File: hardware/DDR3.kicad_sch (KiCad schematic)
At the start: 24 parts, among them U1 NT5CB256M16ER-FL

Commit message: stuff
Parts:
- U1: footprint Package_BGA:FBGA-96_8x13mm_Layout9x16_P0.8mm -> easyeda2kicad:TFBGA-96_L13.0-W8.0-R16-C6-P0.80-TL
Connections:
- net +1V5: now also U1.A2 (DQU5), U1.A3 (DQU7), U1.A7 (DQU4), U1.A9 (VSS), U1.B1 (VSSQ), U1.B3 (VSS), U1.J1 (NC), U1.J2 (VSS), U1.J3 (~{RAS}), U1.J7 (CK), U1.J8 (VSS), U1.J9 (NC), U1.K1 (ODT), U1.K3 (~{CAS_}); no longer U1.C1 (VDDQ), U1.C9 (VDDQ), U1.D2 (VDDQ), U1.D9 (VDD), U1.E9 (VDDQ), U1.F1 (VDDQ), U1.G7 (VDD), U1.H2 (VDDQ), U1.H9 (VDDQ), U1.K8 (VDD), U1.N1 (VDD), U1.N9 (VDD), U1.R1 (VDD), U1.R9 (VDD)
- net A0: now also U1.K8 (VDD); no longer U1.N3 (A0)
- net A1: now also U1.K9 (CKE); no longer U1.P7 (A1)
- net A10: now also U1.M3 (BA2); no longer U1.L7 (A10/AP)
- net A11: now also U1.M7 (NC); no longer U1.R7 (A11)
- net A12: now also U1.M8 (VREFCA); no longer U1.N7 (A12/~{BC})
- net A13: now also U1.M9 (VSS); no longer U1.T3 (A13)
- net A14: now also U1.N1 (VDD); no longer U1.T7 (A14)
- net A2: now also U1.L1 (NC); no longer U1.P3 (A2)
- net A3: now also U1.L2 (~{CS}); no longer U1.N2 (A3)
- net A4: now also U1.L3 (~{WE}); no longer U1.P8 (A4)
- net A5: now also U1.L7 (A10/AP); no longer U1.P2 (A5)
- net A6: now also U1.L8 (ZQ); no longer U1.R8 (A6)
- net A7: now also U1.L9 (NC); no longer U1.R2 (A7)
- net A8: now also U1.M1 (VSS); no longer U1.T8 (A8)
- net A9: now also U1.M2 (BA0); no longer U1.R3 (A9)
- net BA0: no longer U1.M2 (BA0)
- net BA1: no longer U1.N8 (BA1)
- net BA2: no longer U1.M3 (BA2)
- net CASn: no longer U1.K3 (~{CAS_})
- net CKE: no longer U1.K9 (CKE)
- net CKN: no longer U1.K7 (~{CK})
- net CKP: no longer U1.J7 (CK)
- net CSn: no longer U1.L2 (~{CS})
- net DML: no longer U1.E7 (DML)
- net DMU: no longer U1.D3 (DMU)
- net DQL0: now also U1.E1 (VSS); no longer U1.G2 (DQL6)
- net DQL1: now also U1.D9 (VDD); no longer U1.H8 (DQL5)
- net DQL2: now also U1.E2 (VSSQ); no longer U1.H7 (DQL7)
- net DQL3: now also U1.D2 (VDDQ); no longer U1.F7 (DQL1)
- net DQL4: now also U1.D3 (DMU); no longer U1.F2 (DQL2)
- net DQL5: now also U1.D8 (VSSQ); no longer U1.H3 (DQL4)
- net DQL6: now also U1.D1 (VSSQ); no longer U1.E3 (DQL0)
- net DQL7: now also U1.D7 (DQU0); no longer U1.F8 (DQL3)
- net DQSLN: no longer U1.G3 (~{DQSL})
- net DQSLP: no longer U1.F3 (DQSL)
- net DQSUN: no longer U1.B7 (~{DQSU})
- net DQSUP: no longer U1.C7 (DQSU)
- net DQU0: now also U1.C3 (DQU1); no longer U1.A7 (DQU4)
- net DQU1: now also U1.B9 (VSSQ); no longer U1.C3 (DQU1)
- net DQU2: now also U1.C8 (DQU2); no longer U1.B8 (DQU6)
- net DQU4: now also U1.C7 (DQSU); no longer U1.A2 (DQU5)
- net DQU5: now also U1.B8 (DQU6); no longer U1.D7 (DQU0)
- net DQU6: now also U1.C1 (VDDQ); no longer U1.C8 (DQU2)
- net DQU7: now also U1.C9 (VDDQ); no longer U1.A3 (DQU7)
- net GND: no longer U1.A9 (VSS), U1.B1 (VSSQ), U1.B3 (VSS), U1.B9 (VSSQ), U1.D1 (VSSQ), U1.D8 (VSSQ), U1.E1 (VSS), U1.E2 (VSSQ), U1.E8 (VSSQ), U1.F9 (VSSQ), U1.G1 (VSSQ), U1.G8 (VSS), U1.G9 (VSSQ), U1.J1 (NC), U1.J2 (VSS), U1.J8 (VSS), U1.J9 (NC), U1.L1 (NC), U1.L9 (NC), U1.M1 (VSS), U1.M7 (NC), U1.M9 (VSS), U1.P1 (VSS), U1.P9 (VSS), U1.T1 (VSS), U1.T9 (VSS)
- net ODT: no longer U1.K1 (ODT)
- net RASn: no longer U1.J3 (~{RAS})
- net RSTn: no longer U1.T2 (~{RESET})
- net WEn: no longer U1.L3 (~{WE})
- net at C18.2, C19.1, R2.2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: now also U1.N3 (A0); no longer U1.H1 (VREFDQ), U1.M8 (VREFCA)
- net at R1.1: no longer U1.L8 (ZQ)

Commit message: Routing and PCB
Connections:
- net +1V5: now also U1.C1 (VDDQ), U1.C9 (VDDQ), U1.D2 (VDDQ), U1.D9 (VDD), U1.E9 (VDDQ), U1.F1 (VDDQ), U1.G7 (VDD), U1.H2 (VDDQ), U1.H9 (VDDQ), U1.K8 (VDD), U1.N1 (VDD), U1.N9 (VDD), U1.R1 (VDD), U1.R9 (VDD); no longer U1.A2 (DQU5), U1.A3 (DQU7), U1.A7 (DQU4), U1.A9 (VSS), U1.B1 (VSSQ), U1.B3 (VSS), U1.J1 (NC), U1.J2 (VSS), U1.J3 (~{RAS}), U1.J7 (CK), U1.J8 (VSS), U1.J9 (NC), U1.K1 (ODT), U1.K3 (~{CAS_})
- net A0: now also U1.N3 (A0); no longer U1.K8 (VDD)
- net A1: now also U1.P7 (A1); no longer U1.K9 (CKE)
- net A10: now also U1.L7 (A10/AP); no longer U1.M3 (BA2)
- net A11: now also U1.R7 (A11); no longer U1.M7 (NC)
- net A12: now also U1.N7 (A12/~{BC}); no longer U1.M8 (VREFCA)
- net A13: now also U1.T3 (A13); no longer U1.M9 (VSS)
- net A14: now also U1.T7 (A14); no longer U1.N1 (VDD)
- net A2: now also U1.P3 (A2); no longer U1.L1 (NC)
- net A3: now also U1.N2 (A3); no longer U1.L2 (~{CS})
- net A4: now also U1.P8 (A4); no longer U1.L3 (~{WE})
- net A5: now also U1.P2 (A5); no longer U1.L7 (A10/AP)
- net A6: now also U1.R8 (A6); no longer U1.L8 (ZQ)
- net A7: now also U1.R2 (A7); no longer U1.L9 (NC)
- net A8: now also U1.T8 (A8); no longer U1.M1 (VSS)
- net A9: now also U1.R3 (A9); no longer U1.M2 (BA0)
- net BA0: now also U1.M2 (BA0)
- net BA1: now also U1.N8 (BA1)
- net BA2: now also U1.M3 (BA2)
- net CASn: now also U1.K3 (~{CAS})
- net CKE: now also U1.K9 (CKE)
- net CKN: now also U1.K7 (~{CK})
- net CKP: now also U1.J7 (CK)
- net CSn: now also U1.L2 (~{CS})
- net DML: now also U1.E7 (DML)
- net DMU: now also U1.D3 (DMU)
- net DQL0: now also U1.G2 (DQL6); no longer U1.E1 (VSS)
- net DQL1: now also U1.H8 (DQL5); no longer U1.D9 (VDD)
- net DQL2: now also U1.H7 (DQL7); no longer U1.E2 (VSSQ)
- net DQL3: now also U1.F7 (DQL1); no longer U1.D2 (VDDQ)
- net DQL4: now also U1.F2 (DQL2); no longer U1.D3 (DMU)
- net DQL5: now also U1.H3 (DQL4); no longer U1.D8 (VSSQ)
- net DQL6: now also U1.E3 (DQL0); no longer U1.D1 (VSSQ)
- net DQL7: now also U1.F8 (DQL3); no longer U1.D7 (DQU0)
- net DQSLN: now also U1.G3 (~{DQSL})
- net DQSLP: now also U1.F3 (DQSL)
- net DQSUN: now also U1.B7 (~{DQSU})
- net DQSUP: now also U1.C7 (DQSU)
- net DQU0: now also U1.A7 (DQU4); no longer U1.C3 (DQU1)
- net DQU1: now also U1.C3 (DQU1); no longer U1.B9 (VSSQ)
- net DQU2: now also U1.B8 (DQU6); no longer U1.C8 (DQU2)
- net DQU4: now also U1.A2 (DQU5); no longer U1.C7 (DQSU)
- net DQU5: now also U1.D7 (DQU0); no longer U1.B8 (DQU6)
- net DQU6: now also U1.C8 (DQU2); no longer U1.C1 (VDDQ)
- net DQU7: now also U1.A3 (DQU7); no longer U1.C9 (VDDQ)
- net GND: now also U1.A9 (VSS), U1.B1 (VSSQ), U1.B3 (VSS), U1.B9 (VSSQ), U1.D1 (VSSQ), U1.D8 (VSSQ), U1.E1 (VSS), U1.E2 (VSSQ), U1.E8 (VSSQ), U1.F9 (VSSQ), U1.G1 (VSSQ), U1.G8 (VSS), U1.G9 (VSSQ), U1.J1 (NC), U1.J2 (VSS), U1.J8 (VSS), U1.J9 (NC), U1.L1 (NC), U1.L9 (NC), U1.M1 (VSS), U1.M7 (NC), U1.M9 (VSS), U1.P1 (VSS), U1.P9 (VSS), U1.T1 (VSS), U1.T9 (VSS)
- net ODT: now also U1.K1 (ODT)
- net RASn: now also U1.J3 (~{RAS})
- net RSTn: now also U1.T2 (~{RESET})
- net WEn: now also U1.L3 (~{WE})
- net at U1.H1 (VREFDQ): now also C18.2, C19.1, R2.2, R3.1, U1.M8 (VREFCA)
- net at R1.1: now also U1.L8 (ZQ)

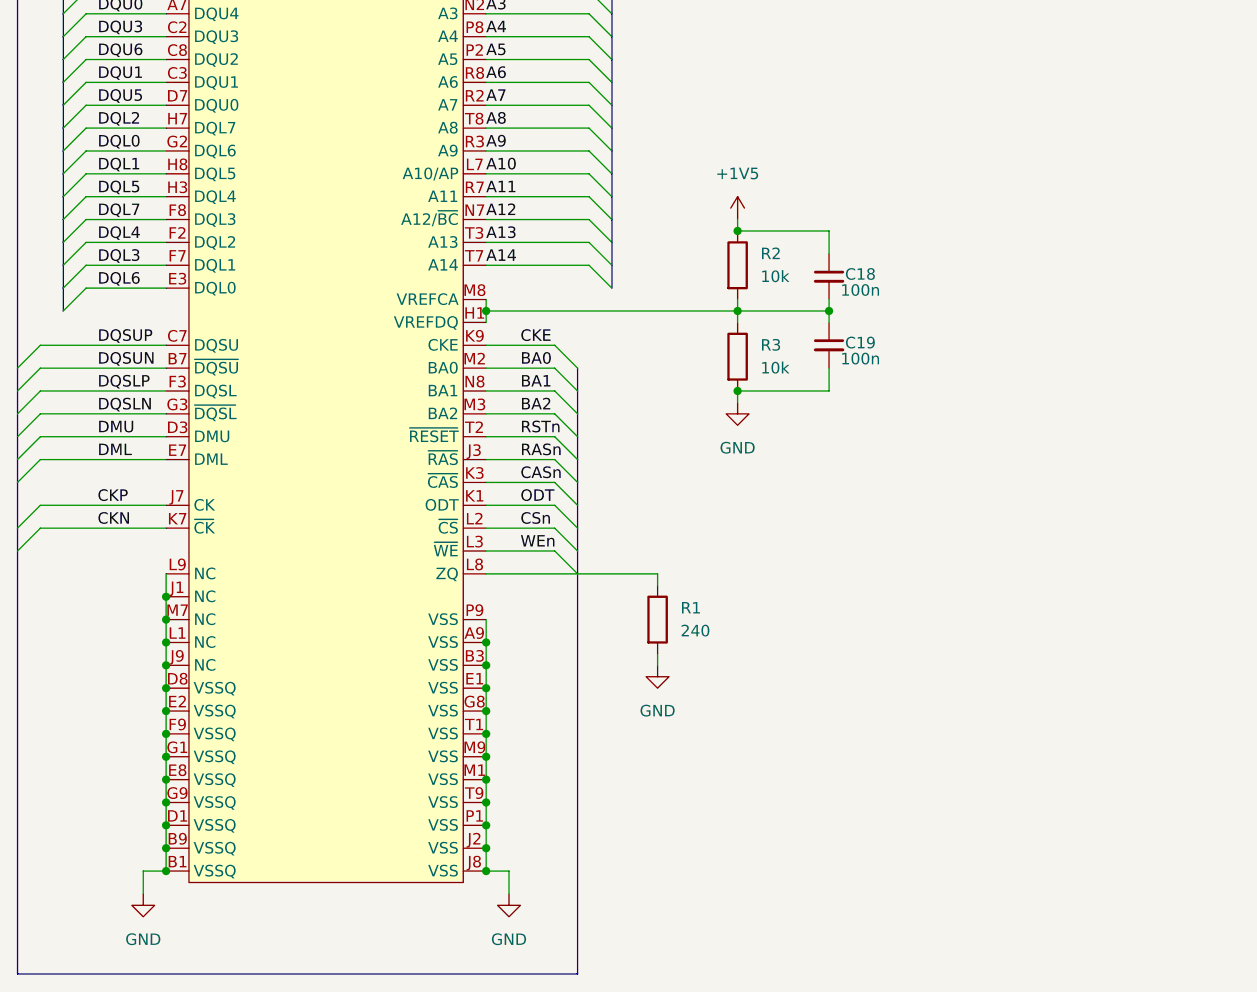
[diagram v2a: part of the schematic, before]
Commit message: component Placement
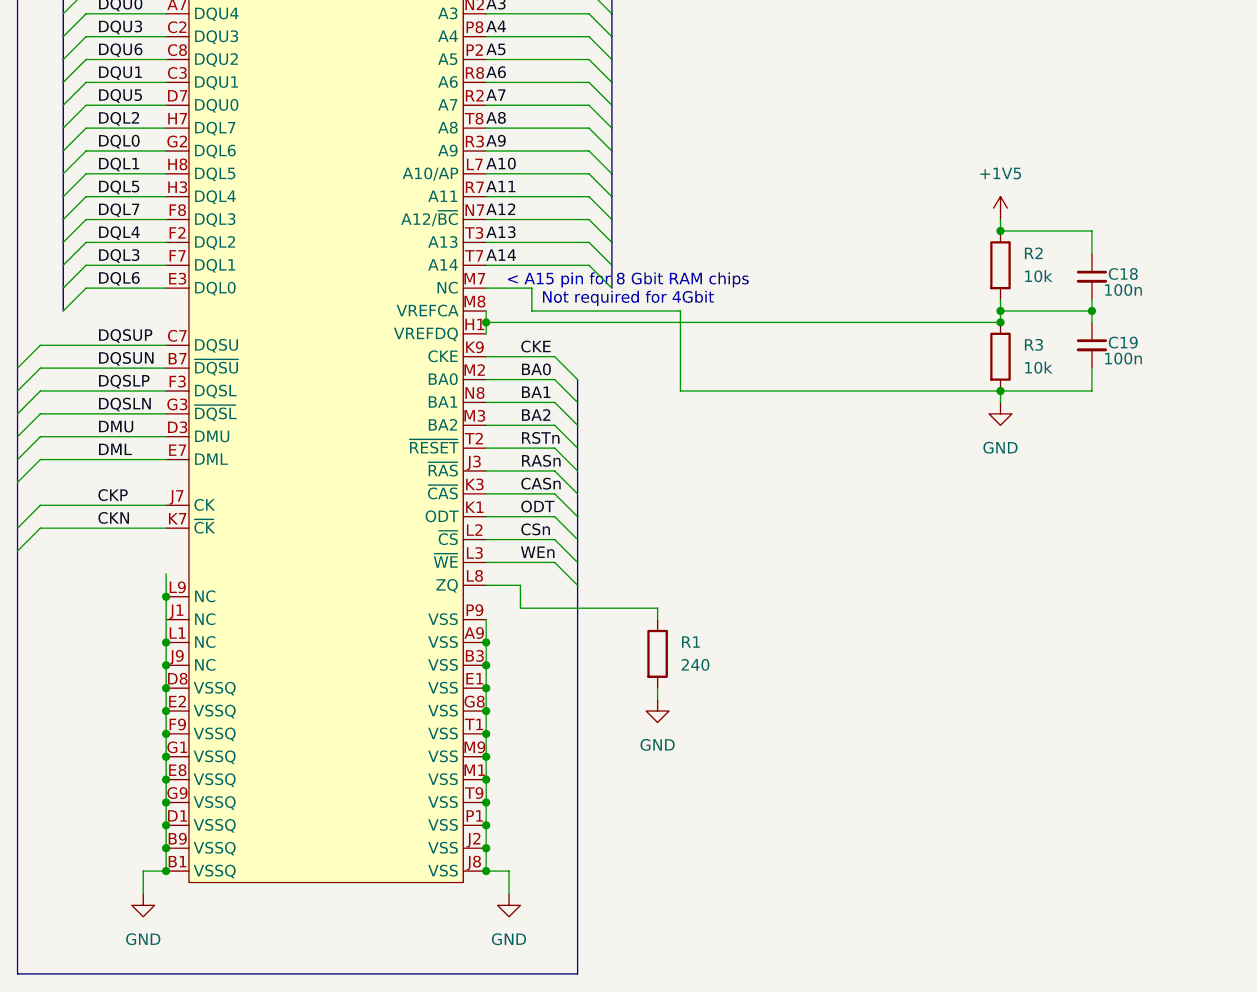
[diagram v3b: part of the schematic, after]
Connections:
- net GND: no longer U1.J1 (NC)
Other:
- note added: "< A15 pin for 8 Gbit RAM chips Not required for 4Gbit"
- moved on the sheet: C18, C19, R1, R2, R3

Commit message: touch up on lots of small things
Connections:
- net GND: now also U1.J1 (NC)
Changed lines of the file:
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@@
-	)
-	(junction
-		(at 129.54 143.51)
-		(diameter 0)
-		(color 0 0 0 0)
 	)
 	(junction
@@
 	(junction
 		(at 226.06 39.37)
+		(diameter 0)
+		(color 0 0 0 0)
+	)
+	(junction
+		(at 129.54 146.05)
 		(diameter 0)
 		(color 0 0 0 0)
@@
 	(wire
 		(pts
-			(xy 129.54 143.51) (xy 129.54 148.59)
-		)
-		(stroke
-			(width 0)
-			(type default)
-		)
-	)
-	(wire
-		(pts
 			(xy 120.65 101.6) (xy 129.54 101.6)
 		)
@@
 		)
 	)
-	(bus
-		(pts
-			(xy 113.03 138.43) (xy 113.03 185.42)
-		)
-		(stroke
-			(width 0)
-			(type default)
-		)
-	)
 	(wire
 		(pts
@@
 		)
 	)
-	(wire
-		(pts
-			(xy 129.54 140.97) (xy 129.54 143.51)
-		)
-		(stroke
-			(width 0)
-			(type default)
-		)
-	)
 	(bus
 		(pts
@@
 	(wire
 		(pts
+			(xy 129.54 146.05) (xy 129.54 148.59)
+		)
+		(stroke
+			(width 0)
+			(type default)
+		)
+	)
+	(wire
+		(pts
 			(xy 165.1 83.82) (xy 176.53 83.82)
 		)
@@
 		)
 		(stroke
+			(width 0)
+			(type default)
+		)
+	)
+	(wire
+		(pts
+			(xy 129.54 143.51) (xy 129.54 146.05)
+		)
+		(stroke
